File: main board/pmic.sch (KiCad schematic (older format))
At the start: 27 parts, among them IC4 MAX20303BEWN+, SW1 SW_Push, U3 SN74LVC1G04YZVR

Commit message: added crystal and motion sensor
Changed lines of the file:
@@
 Text HLabel 1675 3150 0    50   BiDi ~ 0
 P57_SDA
-Text HLabel 1675 3325 0    50   Input ~ 0
+Text HLabel 1675 3325 0    50   BiDi ~ 0
 P37_INT
 Text Label 2150 3325 2    50   ~ 0
@@
 Wire Wire Line
 	9375 1675 9375 1875
-Text HLabel 7625 2300 2    50   BiDi ~ 0
+Text HLabel 7625 2300 2    50   UnSpc ~ 0
 AIN1
 Wire Wire Line
@@
 Text Label 7750 3800 0    50   ~ 0
 P27_MPC0
-Text HLabel 7775 4325 2    50   Output ~ 0
+Text HLabel 7775 4325 2    50   BiDi ~ 0
 P27_MPC0
 Wire Wire Line
@@
 NoConn ~ 4425 3500
 NoConn ~ 4425 4200
+Text HLabel 1650 3900 0    50   Output ~ 0
+3V
+Text Label 2150 3900 2    50   ~ 0
+3V
+Wire Wire Line
+	1650 3900 1800 3900
+$Comp
+L power:PWR_FLAG #FLG0107
+U 1 1 6034D0B8
+P 1800 3900
+F 0 "#FLG0107" H 1800 3975 50  0001 C CNN
+F 1 "PWR_FLAG" H 1800 4073 50  0001 C CNN
+F 2 "" H 1800 3900 50  0001 C CNN
+F 3 "~" H 1800 3900 50  0001 C CNN
+	1    1800 3900
+	-1   0    0    1
+$EndComp
+Connection ~ 1800 3900
+Wire Wire Line
+	1800 3900 2150 3900
 $EndSCHEMATC

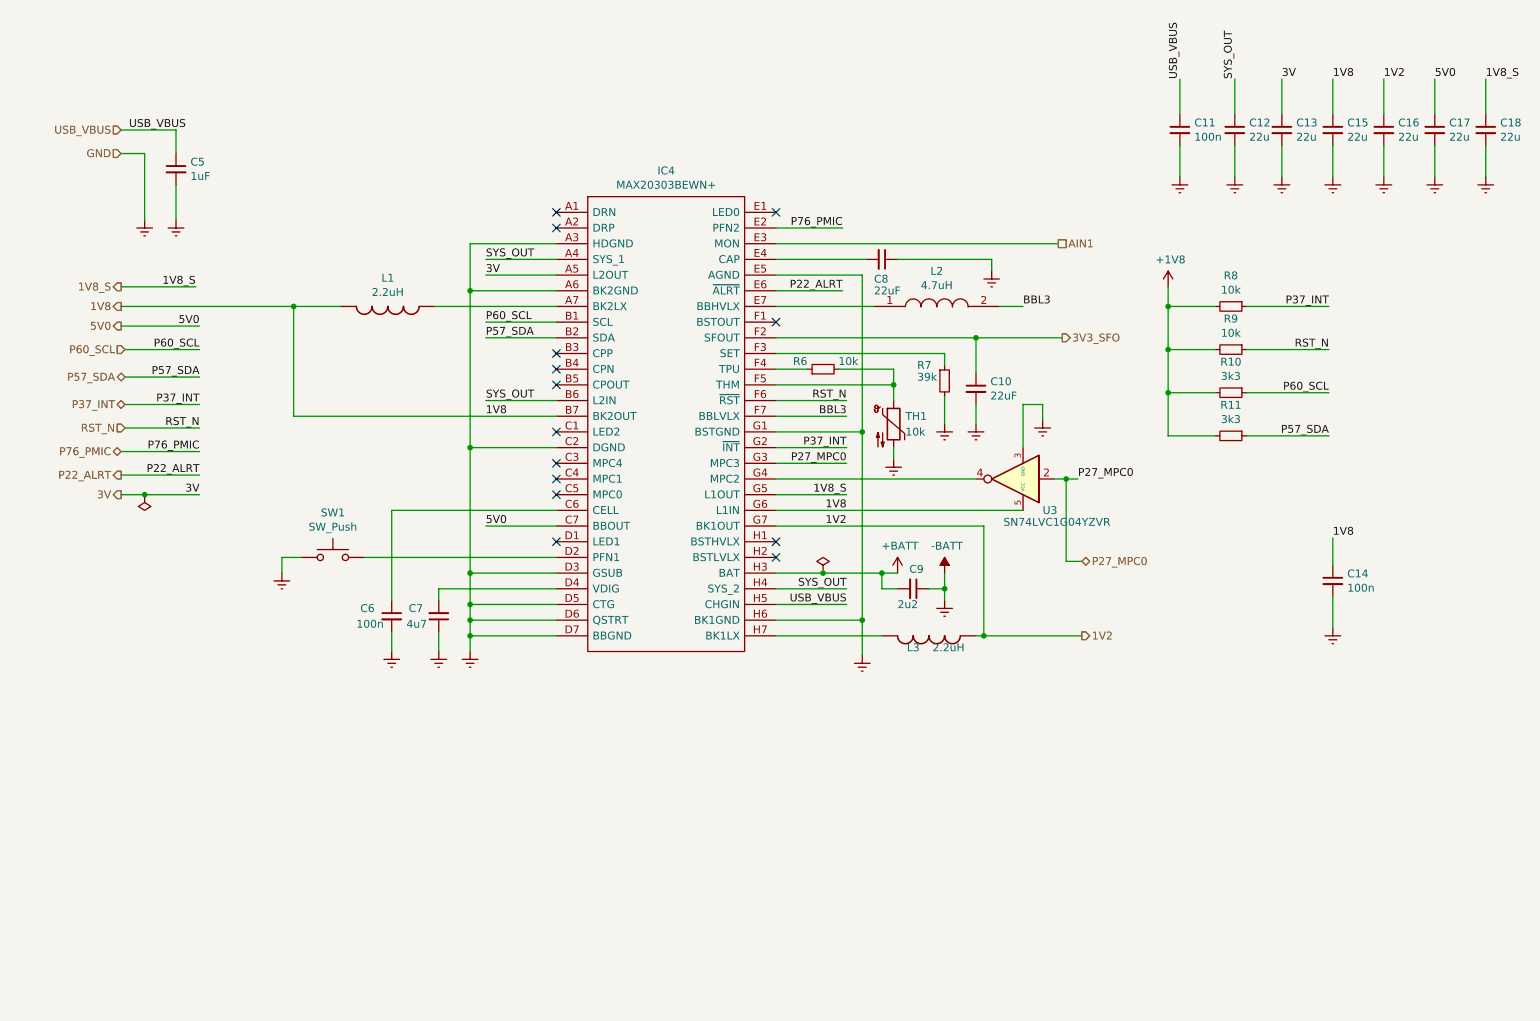
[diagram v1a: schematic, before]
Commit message: added VRTC power input
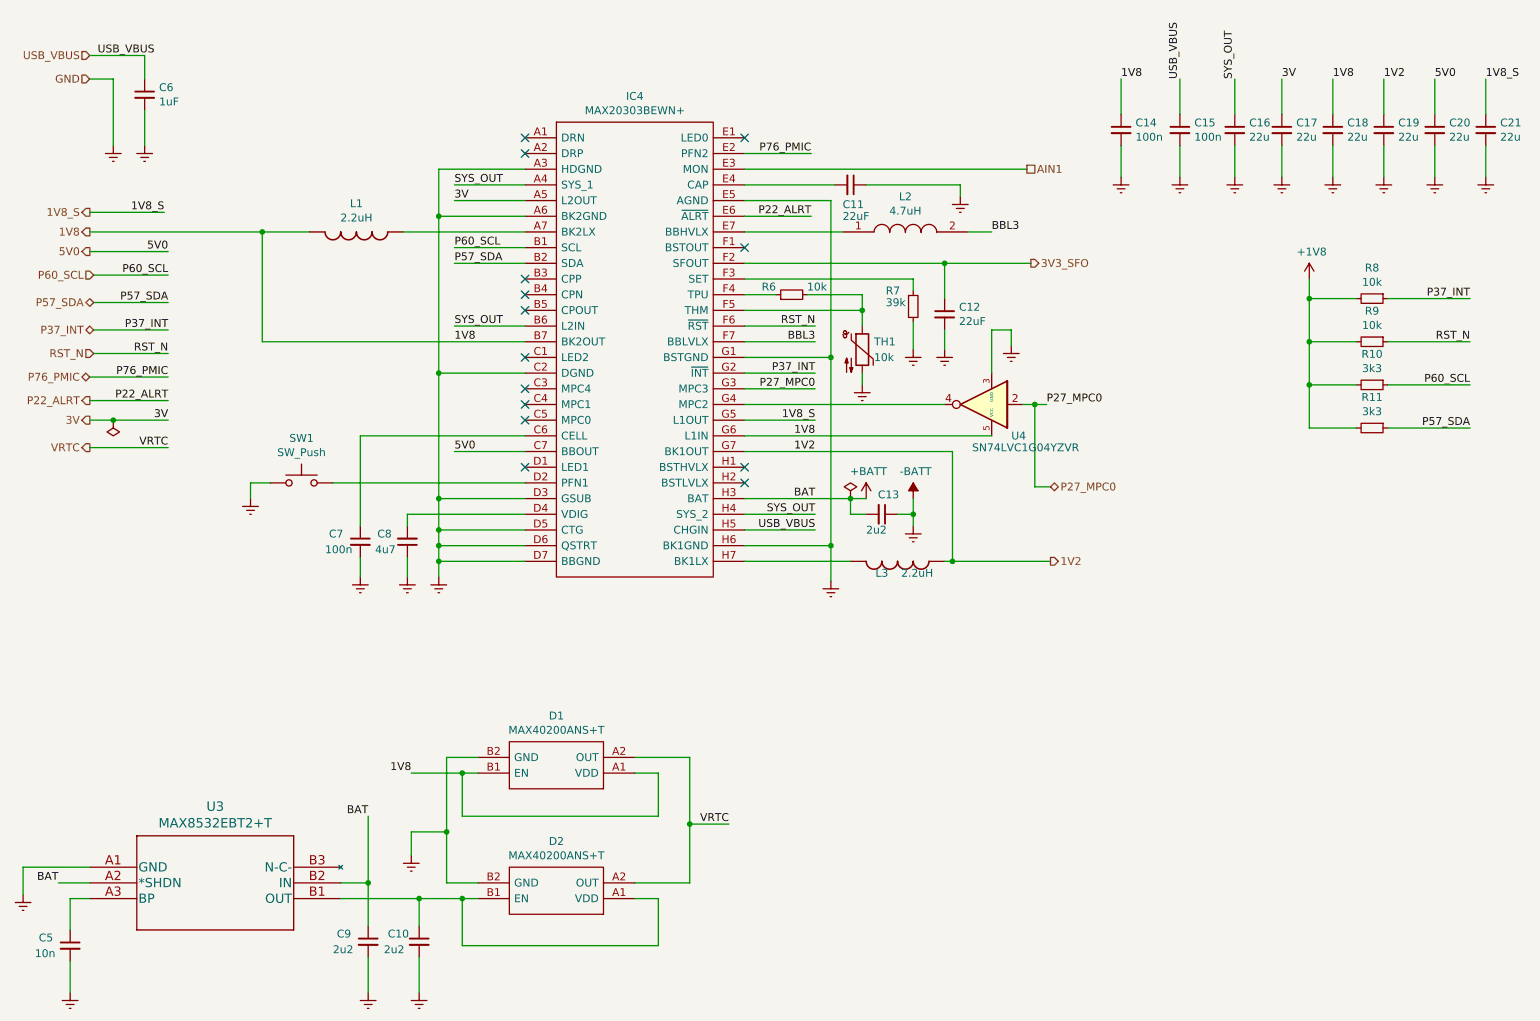
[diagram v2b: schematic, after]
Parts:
- added C10, C9: 2u2, symbol Device:C_Small
- added C5: 10n, symbol Device:C_Small
- added D1, D2: MAX40200ANS+T, Horace:BGA4C35P2X2_73X73X50, symbol Horace:MAX40200ANS+T
- added U3: MAX8532EBT2+T, Horace:MAX8532EBT2&plus_T, symbol Horace:MAX8532EBT2+T
- renumbered C8 to C11, C10 to C12, C9 to C13, C11 to C15, C12 to C16, C13 to C17, C15 to C18, C16 to C19, C17 to C20, C18 to C21, C5 to C6, C6 to C7, C7 to C8, U3 to U4
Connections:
- net +BATT: now also C9.1, U3.A2 (*SHDN), U3.B2 (IN)
- net -BATT: now also C10.2, C5.2, C9.2, D1.B2 (GND), D2.B2 (GND), U3.A1 (GND)
- net 1V8: now also D1.A1 (VDD), D1.B1 (EN)
- new net: C5.1, U3.A3 (BP)
- new net: C10.1, D2.A1 (VDD), D2.B1 (EN), U3.B1 (OUT)
- new net VRTC: D1.A2 (OUT), D2.A2 (OUT)
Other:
- moved on the sheet: C11, C12, C13, C14, C6, C7, C8, IC4, L1, L2, L3, R10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

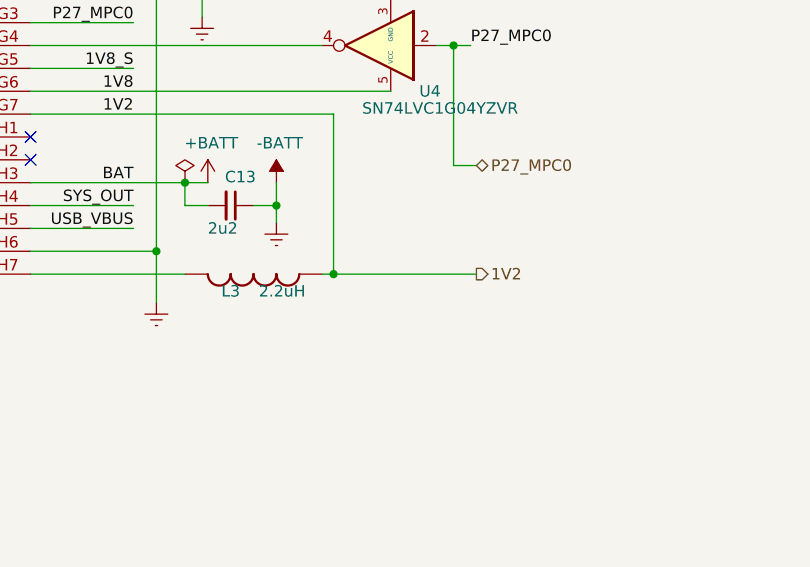
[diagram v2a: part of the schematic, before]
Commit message: added flash and LED
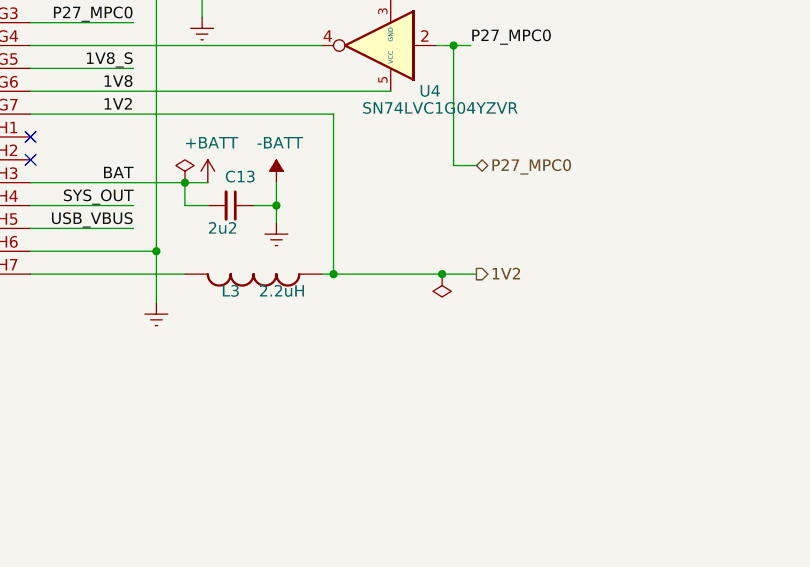
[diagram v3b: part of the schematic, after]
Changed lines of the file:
@@
 Connection ~ 6950 4325
 Wire Wire Line
-	6950 4325 7575 4325
+	6950 4325 7425 4325
 Text Label 9700 1250 0    50   ~ 0
 1V2
@@
 Wire Wire Line
 	1450 3600 1950 3600
+$Comp
+L power:PWR_FLAG #FLG0109
+U 1 1 6087B584
+P 7425 4325
+F 0 "#FLG0109" H 7425 4400 50  0001 C CNN
+F 1 "PWR_FLAG" H 7425 4498 50  0001 C CNN
+F 2 "" H 7425 4325 50  0001 C CNN
+F 3 "~" H 7425 4325 50  0001 C CNN
+	1    7425 4325
+	-1   0    0    1
+$EndComp
+Connection ~ 7425 4325
+Wire Wire Line
+	7425 4325 7575 4325
 $EndSCHEMATC

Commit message: added 100n capacitor
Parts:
- C14, C15, C7: footprint (none) -> Capacitor_SMD:C_0402_1005Metric; Digikey Part Number (none) -> 311-3340-2-ND; Mouser Price/Stock (none) -> https://www.mouser.ee/ProductDetail/Yageo/CC0402KRX5R5BB104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; Price (none) -> 0.09
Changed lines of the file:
@@
 F 0 "C15" H 8492 1621 50  0000 L CNN
 F 1 "100n" H 8492 1530 50  0000 L CNN
-F 2 "" H 8400 1575 50  0001 C CNN
-F 3 "~" H 8400 1575 50  0001 C CNN
+F 2 "Capacitor_SMD:C_0402_1005Metric" H 8400 1575 50  0001 C CNN
+F 3 "https://www.mouser.ee/datasheet/2/447/UPY_GPHC_X5R_4V_to_50V_25-1131599.pdf" H 8400 1575 50  0001 C CNN
+F 4 "https://www.mouser.ee/ProductDetail/Yageo/CC0402KRX5R5BB104/?qs=T%2F3nPWKqOSbG4z8ii3LyCg%3D%3D" H 8400 1575 50  0001 C CNN "Mouser Price/Stock"
+F 5 "311-3340-2-ND" H 8400 1575 50  0001 C CNN "Digikey Part Number"
+F 6 "0.09" H 8400 1575 50  0001 C CNN "Price"
 	1    8400 1575
 	1    0    0    -1
@@
 F 0 "C7" H 2975 4250 50  0000 L CNN
 F 1 "100n" H 2950 4150 50  0000 L CNN
-F 2 "" H 3175 4200 50  0001 C CNN
-F 3 "~" H 3175 4200 50  0001 C CNN
+F 2 "Capacitor_SMD:C_0402_1005Metric" H 3175 4200 50  0001 C CNN
+F 3 "https://www.mouser.ee/datasheet/2/447/UPY_GPHC_X5R_4V_to_50V_25-1131599.pdf" H 3175 4200 50  0001 C CNN
+F 4 "https://www.mouser.ee/ProductDetail/Yageo/CC0402KRX5R5BB104/?qs=T%2F3nPWKqOSbG4z8ii3LyCg%3D%3D" H 3175 4200 50  0001 C CNN "Mouser Price/Stock"
+F 5 "311-3340-2-ND" H 3175 4200 50  0001 C CNN "Digikey Part Number"
+F 6 "0.09" H 3175 4200 50  0001 C CNN "Price"
 	1    3175 4200
 	1    0    0    -1
@@
 F 0 "C14" H 8117 1621 50  0000 L CNN
 F 1 "100n" H 8117 1530 50  0000 L CNN
-F 2 "" H 8025 1575 50  0001 C CNN
-F 3 "~" H 8025 1575 50  0001 C CNN
+F 2 "Capacitor_SMD:C_0402_1005Metric" H 8025 1575 50  0001 C CNN
+F 3 "https://www.mouser.ee/datasheet/2/447/UPY_GPHC_X5R_4V_to_50V_25-1131599.pdf" H 8025 1575 50  0001 C CNN
+F 4 "https://www.mouser.ee/ProductDetail/Yageo/CC0402KRX5R5BB104/?qs=T%2F3nPWKqOSbG4z8ii3LyCg%3D%3D" H 8025 1575 50  0001 C CNN "Mouser Price/Stock"
+F 5 "311-3340-2-ND" H 8025 1575 50  0001 C CNN "Digikey Part Number"
+F 6 "0.09" H 8025 1575 50  0001 C CNN "Price"
 	1    8025 1575
 	1    0    0    -1

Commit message: pmic components
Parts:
- removed SW1: SW_Push, symbol Switch:SW_Push
- added S1: 434153017835, Horace:434153017835, symbol Horace:434153017835
- C10, C13, C9: footprint (none) -> Capacitor_SMD:C_0402_1005Metric; Digikey Part Number (none) -> 311-1682-2-ND; Mouser Price/Stock (none) -> https://www.mouser.ee/ProductDetail/Yageo/CC0402KRX5R5BB225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; Price (none) -> 0.32
- C11, C12: footprint (none) -> Capacitor_SMD:C_0402_1005Metric; Mouser Price/Stock (none) -> https://www.mouser.ee/ProductDetail/Yageo/CC0402MRX5R5BB226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; Price (none) -> 0.38
- C16, C17, C18, C19, C20, C21: value 22u -> 22uF; footprint (none) -> Capacitor_SMD:C_0402_1005Metric; Mouser Price/Stock (none) -> https://www.mouser.ee/ProductDetail/Yageo/CC0402MRX5R5BB226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; Price (none) -> 0.38
- C5: footprint (none) -> Capacitor_SMD:C_0402_1005Metric; Digikey Part Number (none) -> 311-3822-2-ND; Mouser Price/Stock (none) -> https://www.mouser.ee/ProductDetail/Yageo/CC0402MRX7R7BB103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; Price (none) -> 0.09
- C6: footprint (none) -> Capacitor_SMD:C_0402_1005Metric; Digikey Part Number (none) -> 311-1438-2-ND; Mouser Price/Stock (none) -> https://www.mouser.ee/ProductDetail/Yageo/CC0402KRX5R5BB105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; Price (none) -> 0.09
- C8: footprint (none) -> Capacitor_SMD:C_0402_1005Metric; Digikey Part Number (none) -> 311-3476-2-ND; Mouser Price/Stock (none) -> https://www.mouser.ee/ProductDetail/Yageo/CC0402KRX5R5BB475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; Price (none) -> 0.2
- D1, D2: Digikey Part Number (none) -> MAX40200ANS+TTR-ND; Mouser Price/Stock https://www.mouser.co.uk/ProductDetail/Maxim-Integrated/MAX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 -> https://www.mouser.ee/ProductDetail/Maxim-Integrated/MAX402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; Price (none) -> 0.75
- IC4: footprint BGA56C50P7X8_368X418X69 -> Horace:BGA56C50P7X8_368X418X69; Digikey Part Number (none) -> MAX20303BEWN+-ND; Mouser Price/Stock https://www.mouser.co.uk/ProductDetail/Maxim-Integrated/MAX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 -> https://www.mouser.ee/ProductDetail/Maxim-Integrated/MAX203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; Price (none) -> 7.50
- L1, L3: Digikey Part Number (none) -> 490-DFE201612E-2R2M=P2TR-ND; Mouser Price/Stock (none) -> https://www.mouser.ee/ProductDetail/Murata-Electronics/DFE2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; Price (none) -> 0.36
- L2: Digikey Part Number (none) -> 490-18108-2-ND; Price (none) -> 0.35
- R10, R11: footprint (none) -> Resistor_SMD:R_0402_1005Metric; Digikey Part Number (none) -> 541-4080-2-ND; Mouser Price/Stock (none) -> https://www.mouser.ee/ProductDetail/Vishay-Dale/CRCW04023K3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; Price (none) -> 0.09
- R6, R8, R9: footprint (none) -> Resistor_SMD:R_0402_1005Metric; Digikey Part Number (none) -> 541-4276-2-ND; Mouser Price/Stock (none) -> https://www.mouser.ee/ProductDetail/Vishay-Dale/CRCW010010K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; Price (none) -> 0.14
- R7: footprint (none) -> Resistor_SMD:R_0402_1005Metric; Digikey Part Number (none) -> 541-4931-2-ND; Mouser Price/Stock (none) -> https://www.mouser.ee/ProductDetail/Vishay-Dale/CRCW040239K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; Price (none) -> 0.09
- TH1: footprint (none) -> Horace:THRMC0603X33N; Digikey Part Number (none) -> 490-11806-2-ND; Mouser Price/Stock (none) -> https://www.mouser.ee/ProductDetail/Murata-Electronics/NCP0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; Price (none) -> 0.23
- U3: Digikey Part Number (none) -> 2156-MAX8532EBT2+T-ND; Mouser Price/Stock (none) -> https://www.mouser.ee/ProductDetail/Maxim-Integrated/MAX853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; Price (none) -> 0.68
- U4: Digikey Part Number (none) -> 296-21055-2-ND; Mouser Price/Stock (none) -> https://www.mouser.ee/ProductDetail/Texas-Instruments/SN74L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; Price (none) -> 0.44
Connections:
- net +1V8: now also R8.1, R9.1; no longer R8.2, R9.2
- net +BATT: now also C13.1; no longer C13.2
- net -BATT: now also C13.2, S1.2, S1.4; no longer C13.1
- net P37_INT: now also R8.2; no longer R8.1
- net RST_N: now also R9.2; no longer R9.1
- net at IC4.D2 (PFN1): now also S1.1, S1.3
